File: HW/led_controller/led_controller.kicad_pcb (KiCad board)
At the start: 2 copper layers, 100 x 100 mm, 77 parts, among them J1 Conn_01x04_Female, J2 Conn_01x04_Female, J3 Screw_Terminal_01x02, J4 Conn_ARM_JTAG_SWD_10, Q1 BC817, U1 ATSAMD09C, U2 TLC5971PWP

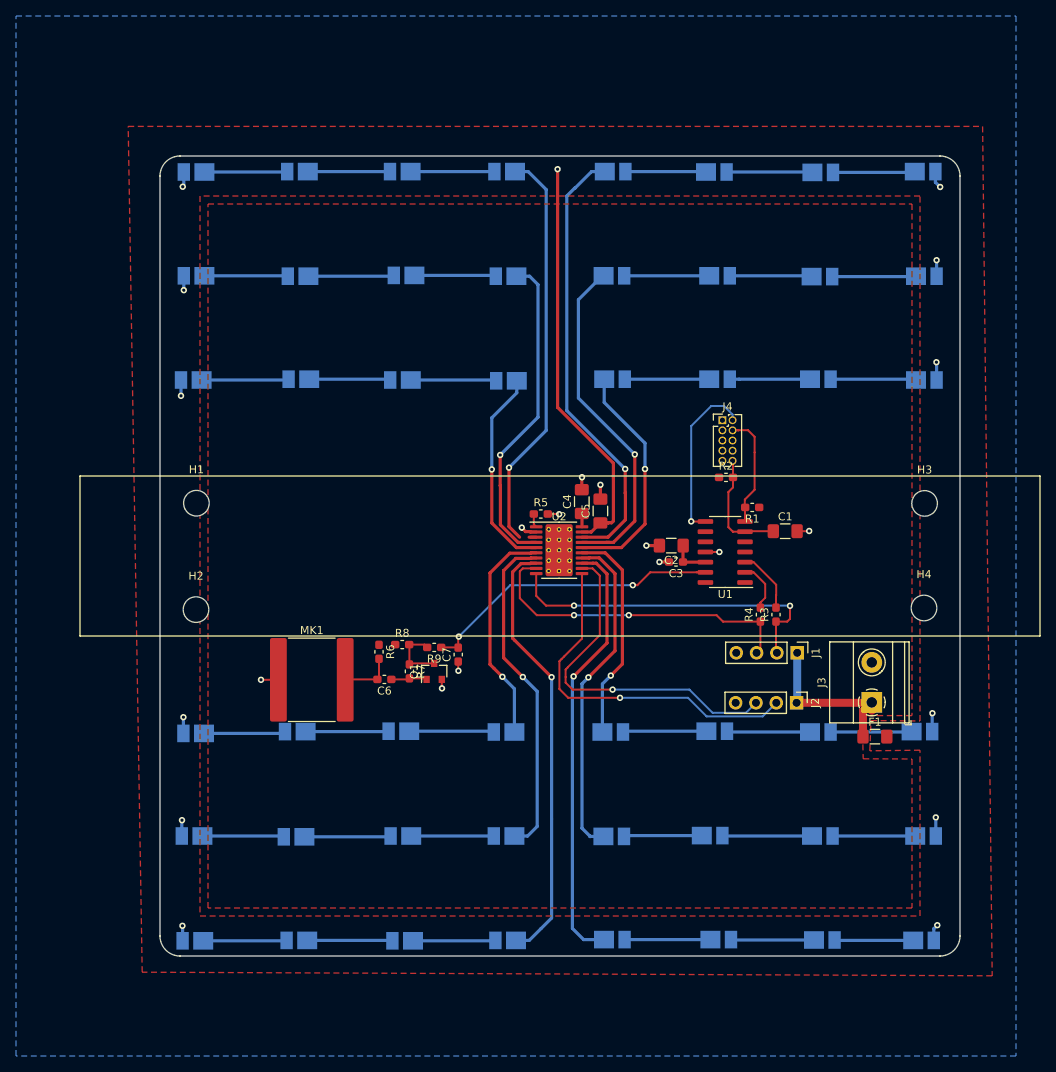
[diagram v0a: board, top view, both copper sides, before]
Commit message: Changing microphone to CMEJ-0415-42-P, mostly finished PCB, DRC passing, adding OSH logo and some text
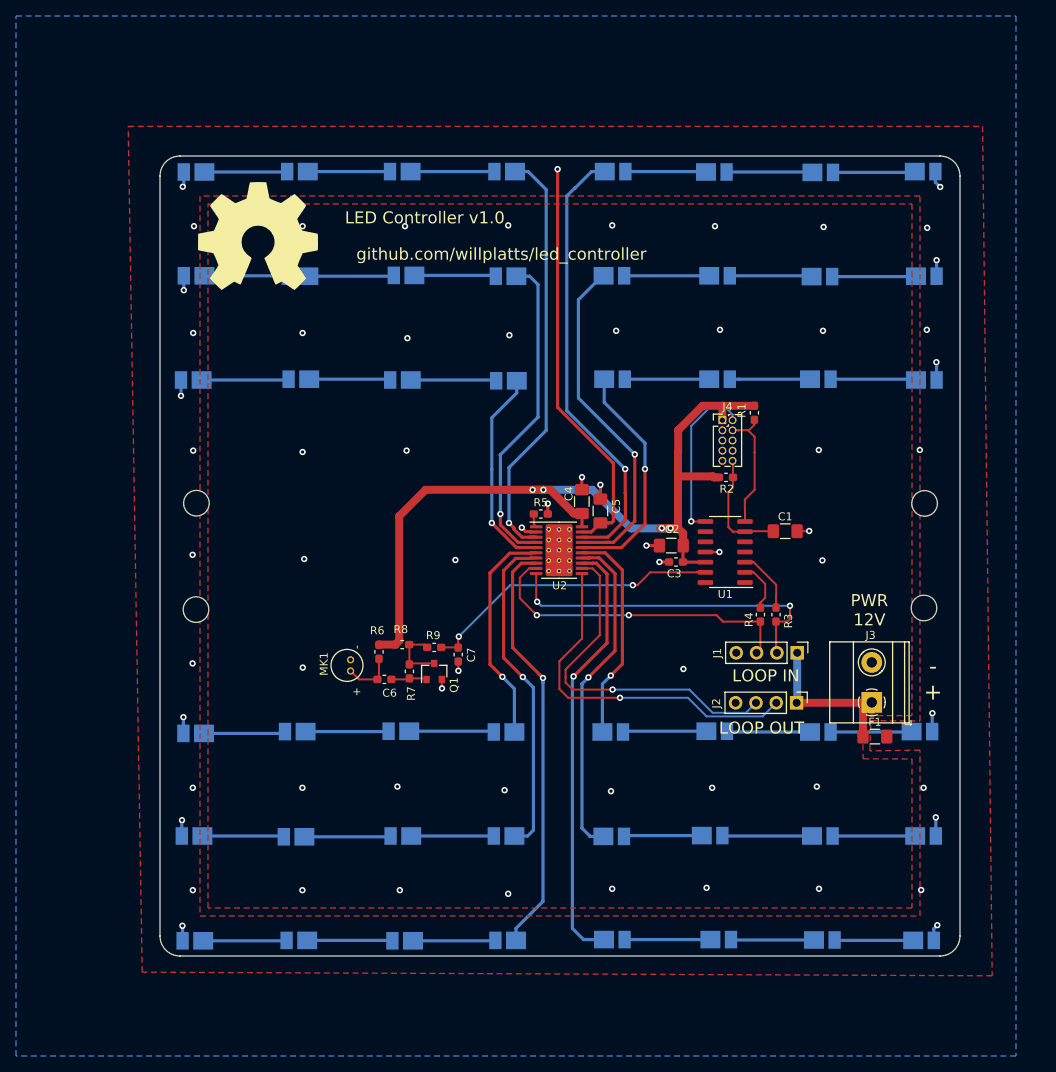
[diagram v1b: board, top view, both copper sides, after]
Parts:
- added G***: OSHW_logo_silkscreen-front_15mm, OSHW_logo:OSHW_logo_silkscreen-front_15mm, F.Cu at (110.2, 47.5)
- MK1: value Microphone -> CMEJ-0415-42-P; footprint Capacitor_SMD:C_3640_9110Metric_Pad2.10x10.45mm_HandSolder -> CMEJ-0415-42-P:MIC_CMEJ-0415-42-P
- moved R1 11.8 mm to (172.3, 69.6), turned to 270 degrees
- moved MK1 4.75 mm to (121.4, 101.2), turned to 90 degrees
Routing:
- net +3V3: track 6.58 -> 104.8 mm, vias 0 -> 4
- net GND: track 17.4 -> 15.1 mm, vias 11 -> 54
- net Net-(D4-Pad1): track 51.6 -> 53.5 mm
- net Net-(D24-Pad1): track 54.3 -> 52.4 mm
- net /SWCLK: track 14.2 -> 15.9 mm
- added copper zone on F.Cu, net GND
- removed copper zone on F.Cu, net +3V3
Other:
- board text added: "- +"
- board text added: "LED Controller v1.0"
- board text added: "LOOP IN"
- board text added: "LOOP OUT"
- board text added: "PWR 12V"
- board text added: "github.com/willplatts/led_controller"
